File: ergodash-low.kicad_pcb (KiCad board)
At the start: 2 copper layers, 178.5 x 150.1 mm, 78 parts, among them J1 Conn_01x02, J2 AudioJack4, SW1 SW_Push, SW10 SW_Push, SW11 SW_Push, SW12 SW_Push, SW13 SW_Push, SW14 SW_Push, SW15 SW_Push, SW16 SW_Push, SW17 SW_Push, SW18 SW_Push, SW19 SW_Push, SW2 SW_Push, SW20 SW_Push, SW21 SW_Push, SW22 SW_Push, SW23 SW_Push, SW24 SW_Push, SW25 SW_Push, SW26 SW_Push, SW27 SW_Push, SW28 SW_Push, SW29 SW_Push, SW3 SW_Push, SW30 SW_Push, SW31 SW_Push, SW32 SW_Push, SW33 SW_Push, SW4 SW_Push, SW5 SW_Push, SW6 SW_Push, SW7 SW_Push, SW8 SW_Push, SW9 SW_Push, U1 ProMicro, U2 ProMicro

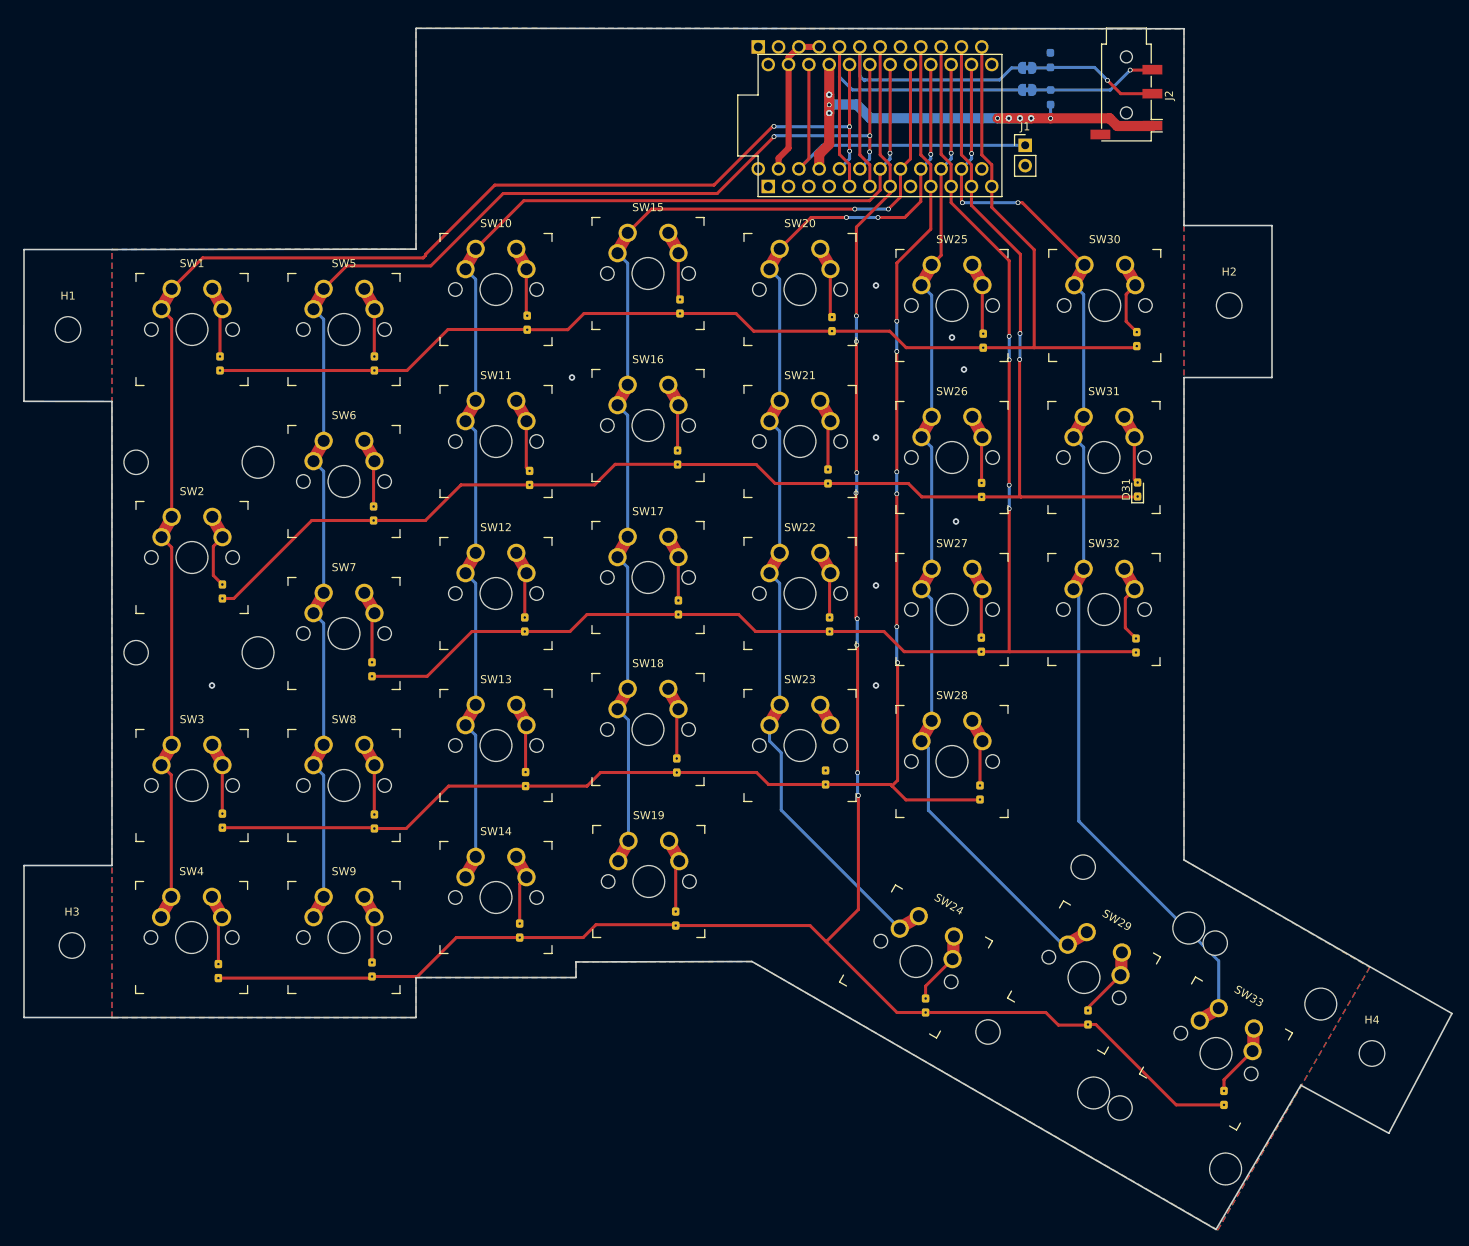
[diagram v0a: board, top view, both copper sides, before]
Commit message: completed schematic and pcb
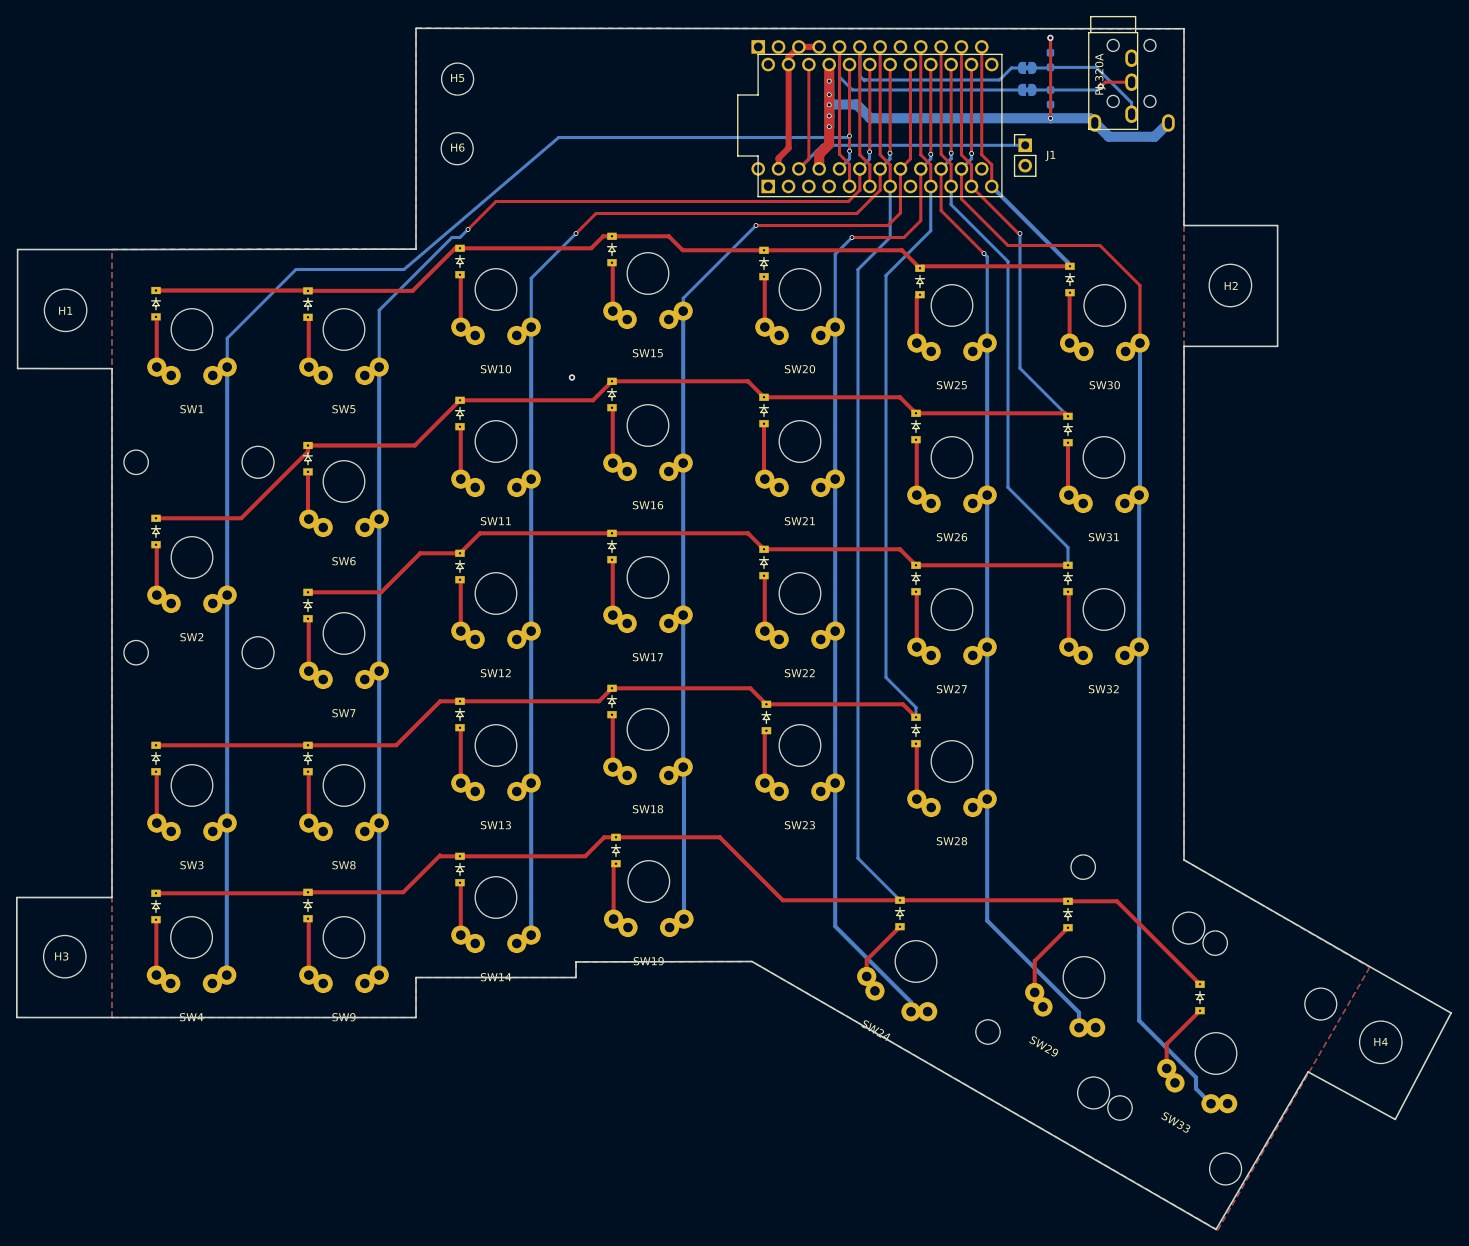
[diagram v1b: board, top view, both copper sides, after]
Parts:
- added H5: MountingHole, MountingHole:MountingHole_4mm, F.Cu at (75.2, 23.7)
- added H6: MountingHole, MountingHole:MountingHole_4mm, F.Cu at (75.2, 32.4)
- D1, D10, D11, D12, D13, D14, D15, D16, D17, D18, D19, D2, D20, D21, D22, D23, D24, D25, D26, D27, D28, D29, D3, D30, D32, D33, D4, D5, D6, D7, D8, D9: footprint local-lib:D_0603_1608Metric_Pad1.05x0.95mm_HandSolder -> local-lib:D_SOD-123-reversible
- D31: footprint local-lib:D_0603_1608Metric_Pad1.05x0.95mm_HandSolder -> local-lib:D_SOD-123-reversible; moved to B.Cu
- H1, H2, H3, H4: footprint MountingHole:MountingHole_3.2mm_M3 -> MountingHole:MountingHole_5.3mm_M5
- J2: footprint Connector_Audio:Jack_3.5mm_PJ320D_Horizontal -> local-lib:TRRS-PJ-320A-dual
- SW1, SW10, SW11, SW12, SW13, SW14, SW15, SW16, SW17, SW18, SW19, SW20, SW21, SW22, SW23, SW24, SW25, SW26, SW27, SW28, SW3, SW30, SW31, SW32, SW4, SW5, SW6, SW7, SW8, SW9: footprint local-lib:SW_MX_reversible -> local-lib:gateron_ks27_reversible
- SW2, SW29, SW33: footprint local-lib:SW_MX_reversible_2u_stab -> local-lib:gateron_ks27_reversible_stabilizer
- U1, U2: footprint local-lib:ProMicro-EnforcedTop -> local-lib:ProMicro
- moved D29 13.1 mm to (151.5, 128.1), turned to -90 degrees
- moved D33 12.9 mm to (168.0, 138.5), turned to -90 degrees
- moved D24 11.9 mm to (130.5, 128.0), turned to -90 degrees
- moved D32 11.9 mm to (151.5, 86.1), turned to -90 degrees
- moved D11 11.9 mm to (75.5, 65.5), turned to -90 degrees
- moved D27 11.6 mm to (132.5, 86.1), turned to -90 degrees
- moved D13 11.5 mm to (75.5, 103.1), turned to -90 degrees
- moved D21 11.5 mm to (113.5, 65.1), turned to -90 degrees
- moved D31 11.5 mm to (151.5, 67.5), turned to -90 degrees
- moved D8 11.4 mm to (56.5, 108.6), turned to -90 degrees
- moved D26 11.4 mm to (132.5, 67.1), turned to -90 degrees
- moved D20 11.4 mm to (113.5, 46.8), turned to -90 degrees
- moved D18 11.4 mm to (94.5, 101.5), turned to -90 degrees
- moved D3 11.4 mm to (37.5, 108.6), turned to -90 degrees
- moved D16 11.4 mm to (94.5, 63.1), turned to -90 degrees
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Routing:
- net /col6: track 130.2 -> 150.2 mm, vias 3 -> 1
- net /col5: track 110.4 -> 128.1 mm, vias 1 -> 2
- net VCC: track 63.3 -> 77.7 mm, vias 8 -> 7
- net /col4: track 120.9 -> 131.1 mm, vias 3 -> 2
- net /row4: track 159.7 -> 150.6 mm
- net /row2: track 179.8 -> 171.1 mm, vias 4 -> 0
- net /col2: track 137.8 -> 146.5 mm, vias 1 -> 2
- net /col1: track 157.7 -> 165.6 mm, vias 3 -> 2
- net /row3: track 182.5 -> 175.1 mm, vias 2 -> 1
- net /col3: track 121.0 -> 128.3 mm, vias 2 -> 1
- net Net-(D23-Pad2): track 0.00 -> 6.63 mm
- net /row1: track 194.1 -> 187.6 mm, vias 6 -> 0
- net /col0: track 176.8 -> 180.7 mm, vias 3 -> 2
- net Net-(D29-Pad2): track 6.11 -> 9.82 mm
- net Net-(J2-PadR2): track 16.1 -> 12.8 mm
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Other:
- board size 178.5 x 150.1 mm -> 179.3 x 150.1 mm
